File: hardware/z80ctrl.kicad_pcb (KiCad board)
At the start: 2 copper layers, 99.8 x 49.9 mm, 31 parts, among them J1 BUS, J2 BUSEXT, J3 ISP, J4 IOADDR, J5 SERIAL1, J6 SERIAL2, J7 Pololu SD, J8 Adafruit SD, J9 CLK/WAIT, SW1 RESET, SW2 HALT, U1 74HCT139, U2 ATMEGA1284P-PU, U3 74HCT02, U4 MCP23S17, Y1 20MHz

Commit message: Experimental SMD stuff
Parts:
- added C8: .1uf, Capacitor_THT:C_Disc_D3.0mm_W1.6mm_P2.50mm, F.Cu at (316.1, 114.9)
- added C9: .1uf, Capacitor_THT:C_Disc_D3.0mm_W1.6mm_P2.50mm, F.Cu at (162.5, 126.6)
- added U5: 74FCT543, Package_SO:SOIC-24W_7.5x15.4mm_P1.27mm, F.Cu at (164.7, 141.1)
- added U6: 74FCT543, Package_SO:SOIC-24W_7.5x15.4mm_P1.27mm, F.Cu at (228.8, 141.1)
- U2: value ATMEGA1284P-PU -> ATmega1284P-AU; footprint Package_DIP:DIP-40_W15.24mm_Socket -> Package_QFP:TQFP-44_10x10mm_P0.8mm
- U4: value MCP23S17 -> 74FCT543; footprint Package_DIP:DIP-28_W7.62mm_Socket -> Package_SO:SOIC-24W_7.5x15.4mm_P1.27mm
- moved C3 92.2 mm to (311.5, 114.9), turned to 0 degrees
- moved C5 81.4 mm to (146.5, 111.4)
- moved C2 73.9 mm to (306.8, 114.9)
- moved J8 61.0 mm to (146.7, 170.9), turned to 0 degrees
- moved J7 58.9 mm to (169.7, 184.3), turned to 0 degrees
- moved C1 45.4 mm to (137.7, 125.6)
- moved Y1 37.5 mm to (196.9, 140.7), turned to 90 degrees
- moved J3 34.5 mm to (130.8, 151.4), turned to 180 degrees
- moved U4 25.3 mm to (184.8, 141.0)
- moved D1 22.7 mm to (187.0, 166.6)
- moved JP2 21.9 mm to (230.8, 161.5)
- moved D3 14.5 mm to (212.0, 160.2)
- moved U2 7.96 mm to (206.7, 138.2), turned to 0 degrees
- moved R2 5.04 mm to (162.2, 117.0), turned to 0 degrees
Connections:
- J2 pad 3: /~RFSH~ -> (no net)
- J7 pad 9: /SDEN -> (no net)
- J9 pad 1: /CLK -> (no net)
- J9 pad 2: Net-(J9-Pad2) -> (no net)
- J9 pad 3: /~MWAIT~ -> (no net)
- SW1 pad 1: GND -> Net-(SW1-Pad1)
- U2 pad 1: /~BUSREQ~ -> /MOSI
- U2 pad 10: VCC -> /TX
- U2 pad 11: GND -> /RX2
- U2 pad 12: Net-(C3-Pad1) -> /TX2
- U2 pad 13: Net-(C2-Pad1) -> /~M1~
- U2 pad 14: /RX -> /~RST~
- U2 pad 15: /TX -> /CLK
- U2 pad 16: /RX2 -> /~INT~
- U2 pad 17: /TX2 -> VCC
- U2 pad 18: /~RD~ -> GND
- U2 pad 19: /~WR~ -> /~BUSACK~
- U2 pad 2: /~IORQ~ -> /MISO
- U2 pad 20: Net-(J9-Pad2) -> /~MREQ~
- U2 pad 21: /~BUSACK~ -> /~HALT~
- U2 pad 22: /D0 -> /~WR~
- U2 pad 23: /D1 -> /~BUSREQ~
- U2 pad 24: /D2 -> /~RD~
- U2 pad 25: /D3 -> /~IORQ~
- U2 pad 26: /D4 -> /~NMI~
- U2 pad 27: /D5 -> VCC
- U2 pad 28: /D6 -> GND
- U2 pad 29: /D7 -> VCC
- U2 pad 3: /~MREQ~ -> /SCK
- U2 pad 30: VCC -> /AD7
- U2 pad 31: GND -> /AD6
- U2 pad 32: VCC -> /AD5
- U2 pad 33: /A7 -> /AD4
- U2 pad 34: /A6 -> /AD3
- U2 pad 35: /A5 -> /AD2
- U2 pad 36: /A4 -> /AD1
- U2 pad 37: /A3 -> /AD0
- U2 pad 38: /A2 -> VCC
- U2 pad 39: /A1 -> GND
- U2 pad 4: /SPIA0 -> /~AVRRST~
- U2 pad 40: /A0 -> /~MWAIT~
- U2 pad 5: /SPIA1 -> VCC
- U2 pad 6: /MOSI -> GND
- U2 pad 7: /MISO -> Net-(C3-Pad1)
- U2 pad 8: /SCK -> Net-(C2-Pad1)
- U2 pad 9: /~AVRRST~ -> /RX
- U4 pad 1: /SDEN -> (no net)
- U4 pad 10: GND -> /A0
- U4 pad 11: /~IOXCS~ -> (no net)
- U4 pad 12: /SCK -> GND
- U4 pad 13: /MOSI -> (no net)
- U4 pad 14: /MISO -> (no net)
- U4 pad 15: GND -> /AD0
- U4 pad 16: GND -> /AD1
- U4 pad 17: GND -> /AD2
- U4 pad 18: /~AVRRST~ -> /AD3
- U4 pad 19: (no net) -> /AD4
- U4 pad 2: /~RFSH~ -> (no net)
- U4 pad 20: (no net) -> /AD5
- U4 pad 21: /A8 -> /AD6
- U4 pad 22: /A9 -> /AD7
- U4 pad 23: /A10 -> (no net)
- U4 pad 24: /A11 -> VCC
- U4 pad 3: /~RST~ -> /A7
- U4 pad 4: /~INT~ -> /A6
- U4 pad 5: /~M1~ -> /A5
- U4 pad 6: Net-(D1-Pad2) -> /A4
- U4 pad 7: /~SDCD~ -> /A3
- U4 pad 8: /~NMI~ -> /A2
- U4 pad 9: VCC -> /A1
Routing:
- net GND: track 296.2 -> 0.00 mm
- net /~AVRRST~: track 169.3 -> 0.00 mm
- net /SCK: track 139.9 -> 0.00 mm
- net /MISO: track 132.9 -> 0.00 mm
- net VCC: track 188.9 -> 58.6 mm, vias 1 -> 0
- net Net-(D1-Pad2): track 128.2 -> 0.00 mm
- net /MOSI: track 126.0 -> 0.00 mm
- net /~IOXCS~: track 122.1 -> 0.00 mm
- net /AD7: track 0.00 -> 111.0 mm
- net /AD6: track 0.00 -> 109.6 mm
- net /AD5: track 0.00 -> 105.4 mm
- net /AD4: track 0.00 -> 101.2 mm
- net /AD3: track 0.00 -> 99.0 mm
- net /AD2: track 0.00 -> 96.7 mm
- net /AD1: track 0.00 -> 93.2 mm
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
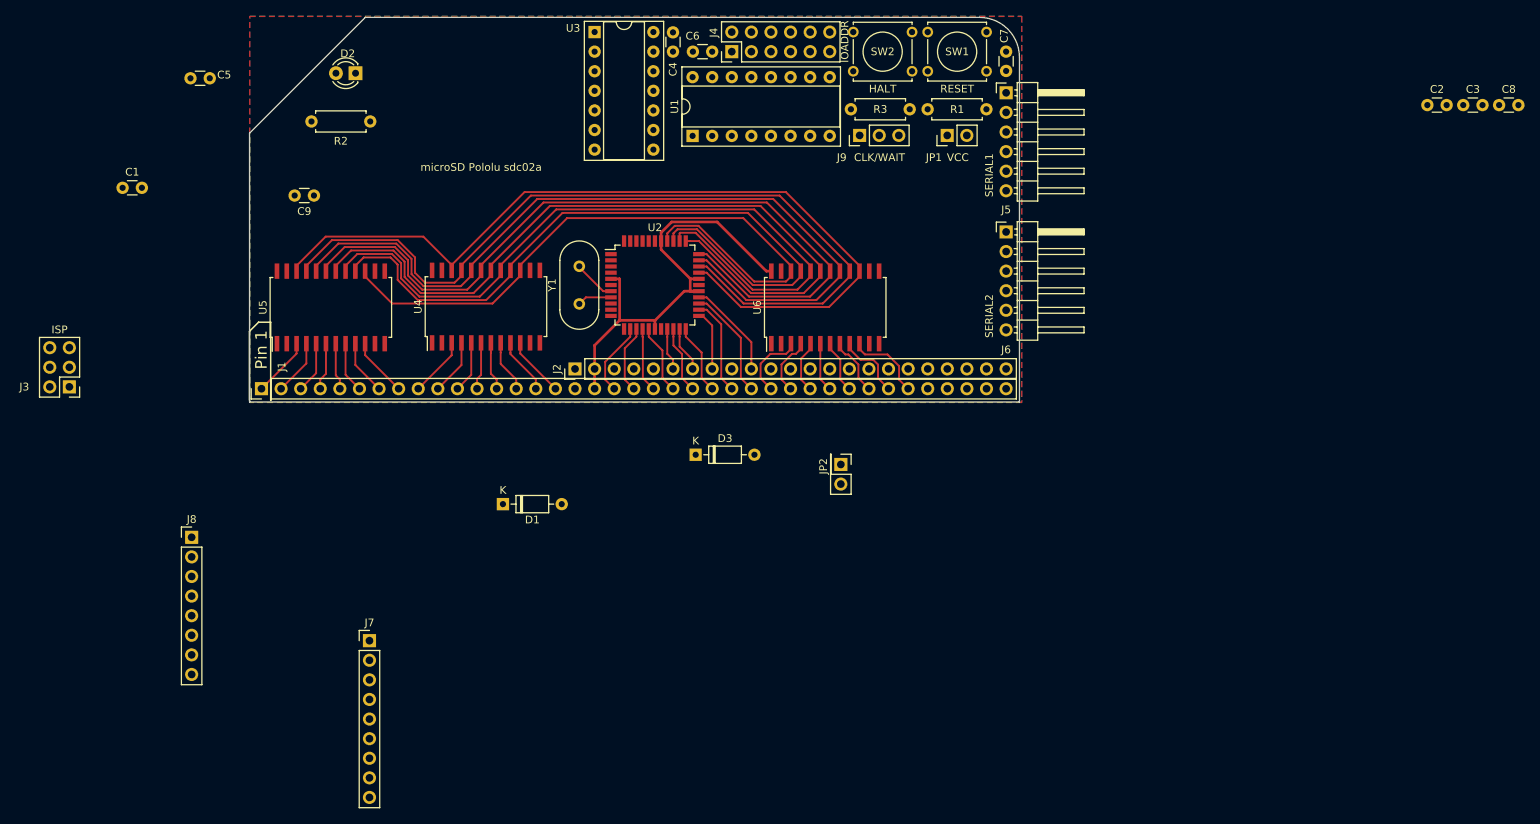
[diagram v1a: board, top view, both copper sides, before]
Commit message: Layout ATmega2560 based SMD board
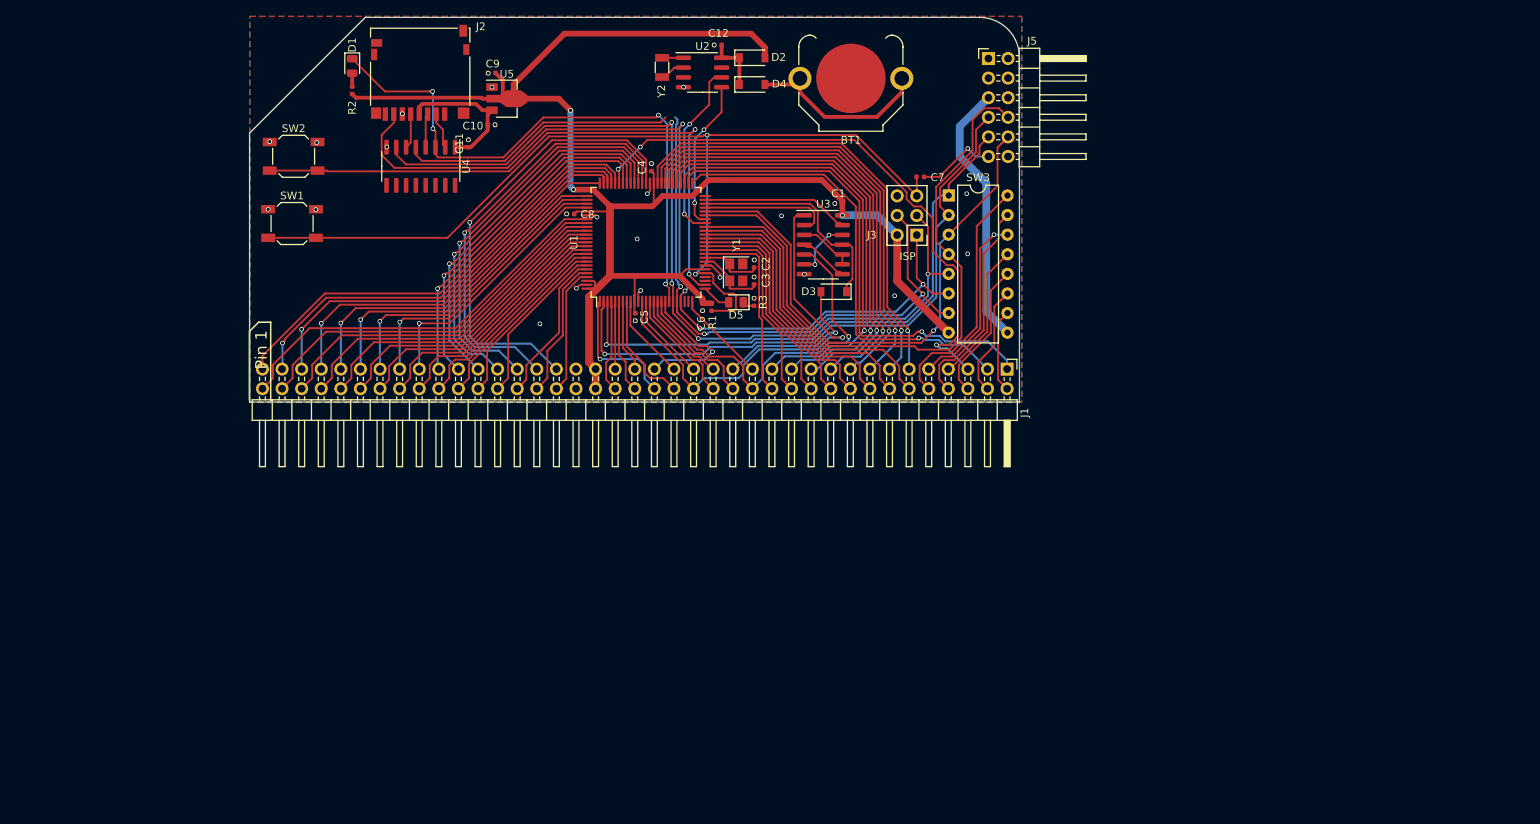
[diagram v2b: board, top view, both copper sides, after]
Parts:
- removed J4: IOADDR, Connector_PinHeader_2.54mm:PinHeader_2x06_P2.54mm_Vertical
- removed J6: SERIAL2, Connector_PinHeader_2.54mm:PinHeader_1x06_P2.54mm_Horizontal
- removed J7: Pololu SD, custom:microSD_Breakout_VR_LS
- removed J8: Adafruit SD, Connector_PinHeader_2.54mm:PinHeader_1x08_P2.54mm_Vertical
- removed J9: CLK/WAIT, Connector_PinHeader_2.54mm:PinHeader_1x03_P2.54mm_Vertical
- removed JP1: VCC, Connector_PinHeader_2.54mm:PinHeader_1x02_P2.54mm_Vertical
- removed JP2: Jumper, Connector_PinHeader_2.54mm:PinHeader_2x01_P2.54mm_Vertical
- removed U6: 74FCT543, Package_SO:SOIC-24W_7.5x15.4mm_P1.27mm
- added BT1: Battery, Battery:BatteryHolder_Keystone_3001_1x12mm, F.Cu at (232.1, 111.4)
- added C10: 10uf, Capacitor_SMD:C_0402_1005Metric, F.Cu at (185.5, 117.4)
- added C11: .1uf, Capacitor_SMD:C_0402_1005Metric, F.Cu at (182.5, 119.8)
- added C12: .1uf, Capacitor_SMD:C_0402_1005Metric, F.Cu at (214.9, 107.1)
- added D4: 1N4148W, Diode_SMD:D_SOD-123, F.Cu at (219.3, 112.2)
- added D5: LED, LED_SMD:LED_0805_2012Metric, F.Cu at (217.2, 140.4)
- added SW3: SW_DIP_x08, Package_DIP:DIP-16_W7.62mm, F.Cu at (244.8, 126.6)
- added Y2: 32.768kHz, Crystal:Crystal_SMD_3215-2Pin_3.2x1.5mm, F.Cu at (207.6, 110.0)
- C1, C2, C3, C4, C5, C6, C7, C8: footprint Capacitor_THT:C_Disc_D3.0mm_W1.6mm_P2.50mm -> Capacitor_SMD:C_0402_1005Metric
- C9: value .1uf -> 10uf; footprint Capacitor_THT:C_Disc_D3.0mm_W1.6mm_P2.50mm -> Capacitor_SMD:C_0402_1005Metric
- D1: value 1N4148 -> LED; footprint Diode_THT:D_DO-35_SOD27_P7.62mm_Horizontal -> LED_SMD:LED_0805_2012Metric
- D2: value LED -> 1N4148W; footprint LED_THT:LED_D3.0mm -> Diode_SMD:D_SOD-123
- D3: value 1N4148 -> 1N4148W; footprint Diode_THT:D_DO-35_SOD27_P7.62mm_Horizontal -> Diode_SMD:D_SOD-123
- J1: footprint Connector_PinHeader_2.54mm:PinHeader_1x39_P2.54mm_Vertical -> Connector_PinHeader_2.54mm:PinHeader_2x39_P2.54mm_Horizontal
- J2: value BUSEXT -> Micro_SD_Card; footprint Connector_PinHeader_2.54mm:PinHeader_1x23_P2.54mm_Vertical -> Connector_Card:microSD_HC_Hirose_DM3D-SF
- J5: footprint Connector_PinHeader_2.54mm:PinHeader_1x06_P2.54mm_Horizontal -> Connector_PinHeader_2.54mm:PinHeader_2x06_P2.54mm_Horizontal
- R1: footprint Resistor_THT:R_Axial_DIN0207_L6.3mm_D2.5mm_P7.62mm_Horizontal -> Resistor_SMD:R_0402_1005Metric
- R2: value 1K -> R; footprint Resistor_THT:R_Axial_DIN0207_L6.3mm_D2.5mm_P7.62mm_Horizontal -> Resistor_SMD:R_0402_1005Metric
- R3: value 10K -> R; footprint Resistor_THT:R_Axial_DIN0207_L6.3mm_D2.5mm_P7.62mm_Horizontal -> Resistor_SMD:R_0402_1005Metric
- SW1, SW2: footprint Button_Switch_THT:SW_Tactile_Straight_KSA0Axx1LFTR -> Button_Switch_SMD:SW_SPST_SKQG_WithoutStem
- U1: value 74HCT139 -> ATmega2560-16AU; footprint Package_DIP:DIP-16_W7.62mm_Socket -> Package_QFP:TQFP-100_14x14mm_P0.5mm
- U2: value ATmega1284P-AU -> PCF8563T; footprint Package_QFP:TQFP-44_10x10mm_P0.8mm -> Package_SO:SOIC-8_3.9x4.9mm_P1.27mm
- U3: value 74HCT02 -> 74HCT00D; footprint Package_DIP:DIP-14_W7.62mm_Socket -> Package_SO:SOIC-14_3.9x8.7mm_P1.27mm
- U4: value 74FCT543 -> 4050; footprint Package_SO:SOIC-24W_7.5x15.4mm_P1.27mm -> Package_SO:SOIC-16_3.9x9.9mm_P1.27mm
- U5: value 74FCT543 -> HT75xx-1-SOT89; footprint Package_SO:SOIC-24W_7.5x15.4mm_P1.27mm -> Package_TO_SOT_SMD:SOT-89-3
- Y1: footprint Crystal:Crystal_HC49-4H_Vertical -> Crystal:Crystal_SMD_3225-4Pin_3.2x2.5mm
- moved C8 121.2 mm to (195.8, 129.0), turned to 180 degrees
- moved J3 111.6 mm to (240.6, 131.7)
- moved J1 96.7 mm to (252.3, 149.1), turned to 270 degrees
- moved C3 94.7 mm to (219.6, 137.6), turned to 90 degrees
- moved C1 92.8 mm to (230.5, 127.6), turned to 180 degrees
- moved C2 89.7 mm to (219.6, 135.4), turned to 90 degrees
- moved SW1 86.1 mm to (159.7, 130.2)
- moved SW2 74.3 mm to (159.9, 121.5)
- moved C5 65.4 mm to (204.2, 142.3), turned to 270 degrees
- moved D1 60.1 mm to (167.5, 109.8), turned to 270 degrees
- moved D2 51.4 mm to (219.3, 108.7), turned to 0 degrees
- moved R1 43.9 mm to (214.0, 141.0), turned to 270 degrees
- moved J2 43.3 mm to (176.3, 110.7), turned to 0 degrees
- moved U3 40.5 mm to (228.5, 133.0)
- moved U5 35.1 mm to (187.1, 114.0), turned to 0 degrees
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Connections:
- D1 pad 1: /~HALT~ -> /~SDCS~
- D2 pad 1: /~SDCS~ -> Net-(C12-Pad1)
- D2 pad 2: Net-(D2-Pad2) -> VCC
- D3 pad 1: Net-(D3-Pad1) -> /~WAIT2~
- J1 pad 1: /A15 -> /USER3
- J1 pad 10: /A6 -> /TXB
- J1 pad 11: /A5 -> /D15
- J1 pad 12: /A4 -> /D7
- J1 pad 13: /A3 -> /D14
- J1 pad 14: /A2 -> /D6
- J1 pad 15: /A1 -> /D13
- J1 pad 16: /A0 -> /D5
- J1 pad 17: GND -> /D12
- J1 pad 18: VCC -> /D4
- J1 pad 19: /~M1~ -> /D11
- J1 pad 2: /A14 -> /USER7
- J1 pad 20: /~RST~ -> /D3
- J1 pad 21: /CLK -> /D10
- J1 pad 22: /~INT~ -> /D2
- J1 pad 23: /~MREQ~ -> /D9
- J1 pad 24: /~WR~ -> /D1
- J1 pad 25: /~RD~ -> /D8
- J1 pad 26: /~IORQ~ -> /D0
- J1 pad 27: /D0 -> /~NMI~
- J1 pad 28: /D1 -> /~IORQ~
- J1 pad 29: /D2 -> /~WAIT~
- J1 pad 3: /A13 -> /USER2
- J1 pad 30: /D3 -> /~RD~
- J1 pad 31: /D4 -> /~BUSREQ~
- J1 pad 32: /D5 -> /~WR~
- J1 pad 33: /D6 -> /~HALT~
- J1 pad 34: /D7 -> /~MREQ~
- J1 pad 35: /TX -> /~BUSACK~
- J1 pad 36: /RX -> /~INT~
- J1 pad 37: /SCK -> /CLK2
- J1 pad 38: /MISO -> /CLK
- J1 pad 39: /MOSI -> /~RST2~
- J1 pad 4: /A12 -> /USER6
- J1 pad 5: /A11 -> /USER1
- J1 pad 6: /A10 -> /USER5
- J1 pad 7: /A9 -> /RX2B
- J1 pad 8: /A8 -> /RXB
- J1 pad 9: /A7 -> /TX2B
- J2 pad 1: GND -> (no net)
- J2 pad 10: /~NMI~ -> (no net)
- J2 pad 2: VCC -> Net-(J2-Pad2)
- J2 pad 3: (no net) -> Net-(J2-Pad3)
- J2 pad 4: (no net) -> /3V3
- J2 pad 5: (no net) -> Net-(J2-Pad5)
- J2 pad 6: /~BUSACK~ -> GND
- J2 pad 7: /~HALT~ -> /MISO
- J2 pad 8: /~BUSREQ~ -> (no net)
- J2 pad 9: /~WAIT~ -> (no net)
- J5 pad 2: (no net) -> GND
- J5 pad 3: Net-(J5-Pad3) -> (no net)
- J5 pad 4: /RX -> (no net)
- J5 pad 5: /TX -> /VCCS
- J5 pad 6: Net-(C7-Pad1) -> (no net)
- R2 pad 1: Net-(D2-Pad2) -> VCC
- R2 pad 2: VCC -> Net-(D1-Pad2)
- R3 pad 1: VCC -> GND
- R3 pad 2: /~MWAIT~ -> Net-(D5-Pad1)
- SW1 pad 1: Net-(SW1-Pad1) -> GND
- SW2 pad 2: Net-(D1-Pad2) -> Net-(SW2-Pad2)
- U1 pad 1: /~IORQ~ -> /CLK
- U1 pad 10: /~AUXCS1~ -> VCC
- U1 pad 11: /~SDCS~ -> GND
- U1 pad 12: /~IOXCS~ -> /~MREQ~
- U1 pad 13: /SPIA1 -> /~HALT~
- U1 pad 14: /SPIA0 -> /~WR~
- U1 pad 15: GND -> /~BUSREQ~
- U1 pad 16: VCC -> /~RD~
- U1 pad 2: /A6 -> /RX
- U1 pad 3: /A7 -> /TX
- U1 pad 4: Net-(J4-Pad3) -> /~M1~
- U1 pad 5: Net-(J4-Pad5) -> /~RFSH~
- U1 pad 6: Net-(J4-Pad7) -> /~RST~
- U1 pad 7: Net-(J4-Pad9) -> /~RST2~
- U1 pad 8: GND -> /~INT~
- U1 pad 9: /~AUXCS2~ -> /~BUSACK~
- U2 pad 1: /MOSI -> Net-(U2-Pad1)
- U2 pad 2: /MISO -> Net-(U2-Pad2)
- U2 pad 3: /SCK -> (no net)
- U2 pad 4: /~AVRRST~ -> GND
- U2 pad 5: VCC -> /SCL
- U2 pad 6: GND -> /SDA
- U2 pad 7: Net-(C3-Pad1) -> (no net)
- U2 pad 8: Net-(C2-Pad1) -> Net-(C12-Pad1)
- U3 pad 1: Net-(U3-Pad1) -> /~MREQ~
- U3 pad 11: Net-(U3-Pad11) -> /~WAIT2~
- U3 pad 12: Net-(U3-Pad10) -> Net-(U3-Pad12)
- U3 pad 13: Net-(D3-Pad1) -> /~WAITCLR~
- U3 pad 2: /~BUSREQ~ -> /~MWAIT~
- U3 pad 3: /~BUSREQ~ -> Net-(U3-Pad10)
- U3 pad 4: Net-(U3-Pad11) -> Net-(U3-Pad4)
- U3 pad 5: Net-(U3-Pad1) -> /~IORQ~
- U3 pad 6: Net-(J4-Pad10) -> Net-(U3-Pad12)
- U3 pad 8: /~MREQ~ -> Net-(U3-Pad4)
- U3 pad 9: /~MWAIT~ -> Net-(U3-Pad10)
- U4 pad 1: (no net) -> /3V3
- U4 pad 10: /A0 -> (no net)
- U4 pad 11: (no net) -> GND
- U4 pad 12: GND -> (no net)
- U4 pad 14: (no net) -> GND
- U4 pad 15: /AD0 -> (no net)
- U4 pad 16: /AD1 -> (no net)
- U4 pad 2: (no net) -> Net-(J2-Pad2)
- U4 pad 3: /A7 -> /~SDCS~
- U4 pad 4: /A6 -> Net-(J2-Pad3)
- U4 pad 5: /A5 -> /MOSI
- U4 pad 6: /A4 -> Net-(J2-Pad5)
- U4 pad 7: /A3 -> /SCK
- U4 pad 8: /A2 -> GND
- U4 pad 9: /A1 -> GND
- U5 pad 1: (no net) -> GND
- U5 pad 2: (no net) -> VCC
- U5 pad 3: /A15 -> /3V3
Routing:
- net VCC: track 58.6 -> 207.5 mm, vias 0 -> 3
- net /~AVRRST~: track 0.00 -> 126.0 mm, vias 0 -> 2
- net /MISO: track 0.00 -> 118.4 mm, vias 0 -> 4
- net /SCK: track 0.00 -> 114.7 mm, vias 0 -> 4
- net /MOSI: track 0.00 -> 113.2 mm, vias 0 -> 3
- net /AD7: track 111.0 -> 0.00 mm
- net /AD6: track 109.6 -> 0.00 mm
- net /AD5: track 105.4 -> 0.00 mm
- net /AD4: track 101.2 -> 0.00 mm
- net /AD3: track 99.0 -> 0.00 mm
- net /AD2: track 96.7 -> 0.00 mm
- net /AD1: track 93.2 -> 0.00 mm
- net /AD0: track 87.4 -> 0.00 mm
- net /RX2: track 0.00 -> 82.9 mm
- net /RX: track 0.00 -> 80.2 mm, vias 0 -> 1
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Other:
- board text added: "z80ctrl SMD1 (C)2020 J.B. Langston https://github.com/jblang/z80ctrl"
- board text removed: "J4: IO addresses - None (left) - 00-3F - 40-7F - 80-BF - C0-FF - 00-FF (right) JP1: VCC from SERIAL1 JP2: RESET for IO expander"
- board text removed: "microSD Pololu sdc02a"
- board text removed: "z80ctrl REV4 (C)2018 J.B. Langston https://github.com/jblang/z80ctrl"
